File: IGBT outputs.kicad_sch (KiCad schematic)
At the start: 8 parts, among them Q1 NGD8201AN, Q2 NGD8201AN, Q3 NGD8201AN, Q4 NGD8201AN, Q5 NGD8201AN, Q6 NGD8201AN, Q7 NGD8201AN, Q8 NGD8201AN

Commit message: All fixed up for JLC
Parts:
- Q1, Q2, Q3, Q4, Q6, Q7, Q8: LCSC (none) -> C151649
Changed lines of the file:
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@@
+      (effects (font (size 1.27 1.27)) hide)
+    )
+    (property "LCSC" "C151649" (id 4) (at 139.7 119.38 0)
       (effects (font (size 1.27 1.27)) hide)
     )
@@
       (effects (font (size 1.27 1.27)) hide)
     )
+    (property "LCSC" "C151649" (id 4) (at 152.4 81.28 0)
+      (effects (font (size 1.27 1.27)) hide)
+    )
     (pin "1")
     (pin "2")
@@
     )
     (property "Datasheet" "~" (id 3) (at 139.7 64.77 0)
+      (effects (font (size 1.27 1.27)) hide)
+    )
+    (property "LCSC" "C151649" (id 4) (at 139.7 64.77 0)
       (effects (font (size 1.27 1.27)) hide)
     )
@@
       (effects (font (size 1.27 1.27)) hide)
     )
+    (property "LCSC" "C151649" (id 4) (at 139.7 99.06 0)
+      (effects (font (size 1.27 1.27)) hide)
+    )
     (pin "1")
     (pin "2")
@@
       (effects (font (size 1.27 1.27)) hide)
     )
+    (property "LCSC" "C151649" (id 4) (at 139.7 81.28 0)
+      (effects (font (size 1.27 1.27)) hide)
+    )
     (pin "1")
     (pin "2")
@@
     )
     (property "Datasheet" "~" (id 3) (at 152.4 99.06 0)
+      (effects (font (size 1.27 1.27)) hide)
+    )
+    (property "LCSC" "C151649" (id 4) (at 152.4 99.06 0)
       (effects (font (size 1.27 1.27)) hide)
     )
@@
       (effects (font (size 1.27 1.27)) hide)
     )
+    (property "LCSC" "C151649" (id 4) (at 152.4 119.38 0)
+      (effects (font (size 1.27 1.27)) hide)
+    )

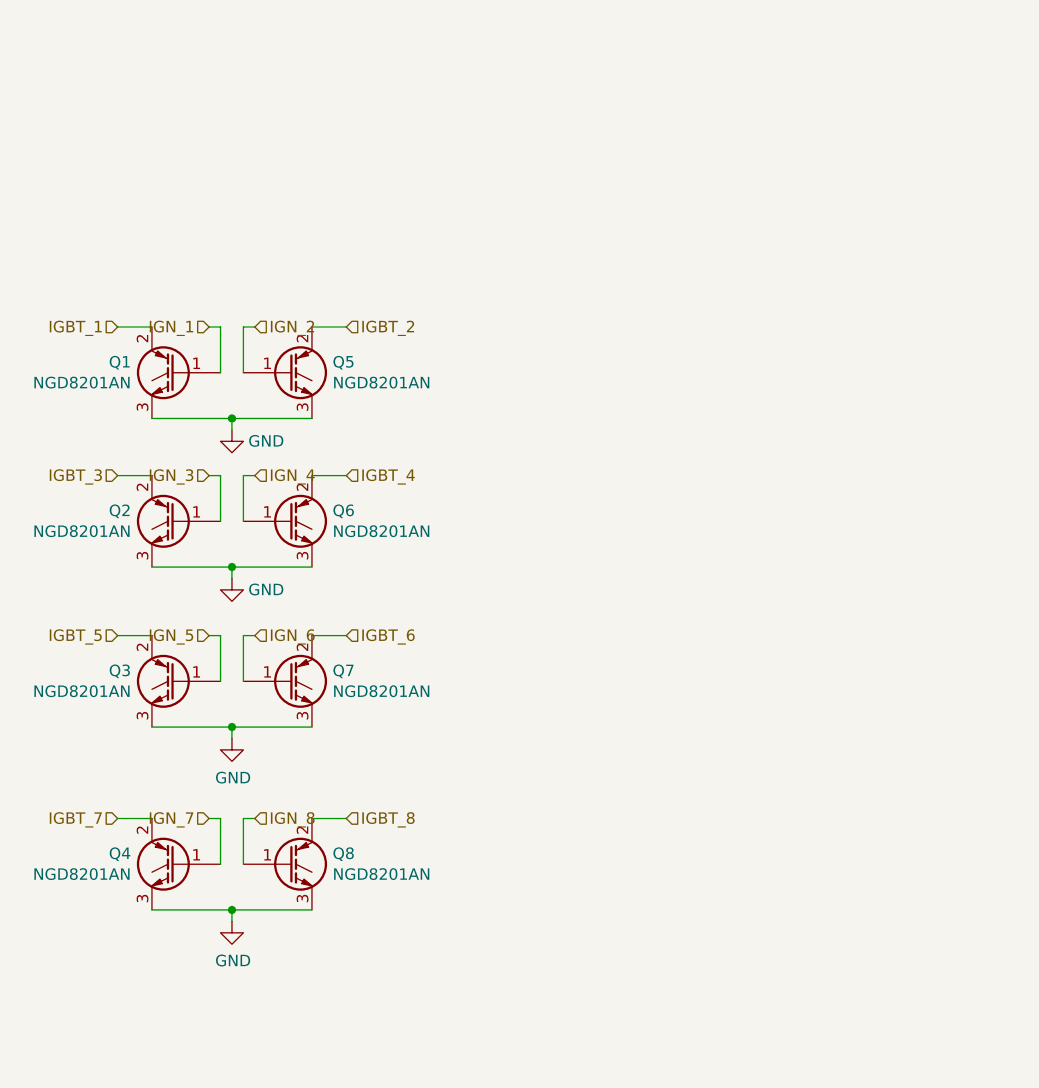
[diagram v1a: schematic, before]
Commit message: convert to kicad7, add jumpers for direct drive igbt output
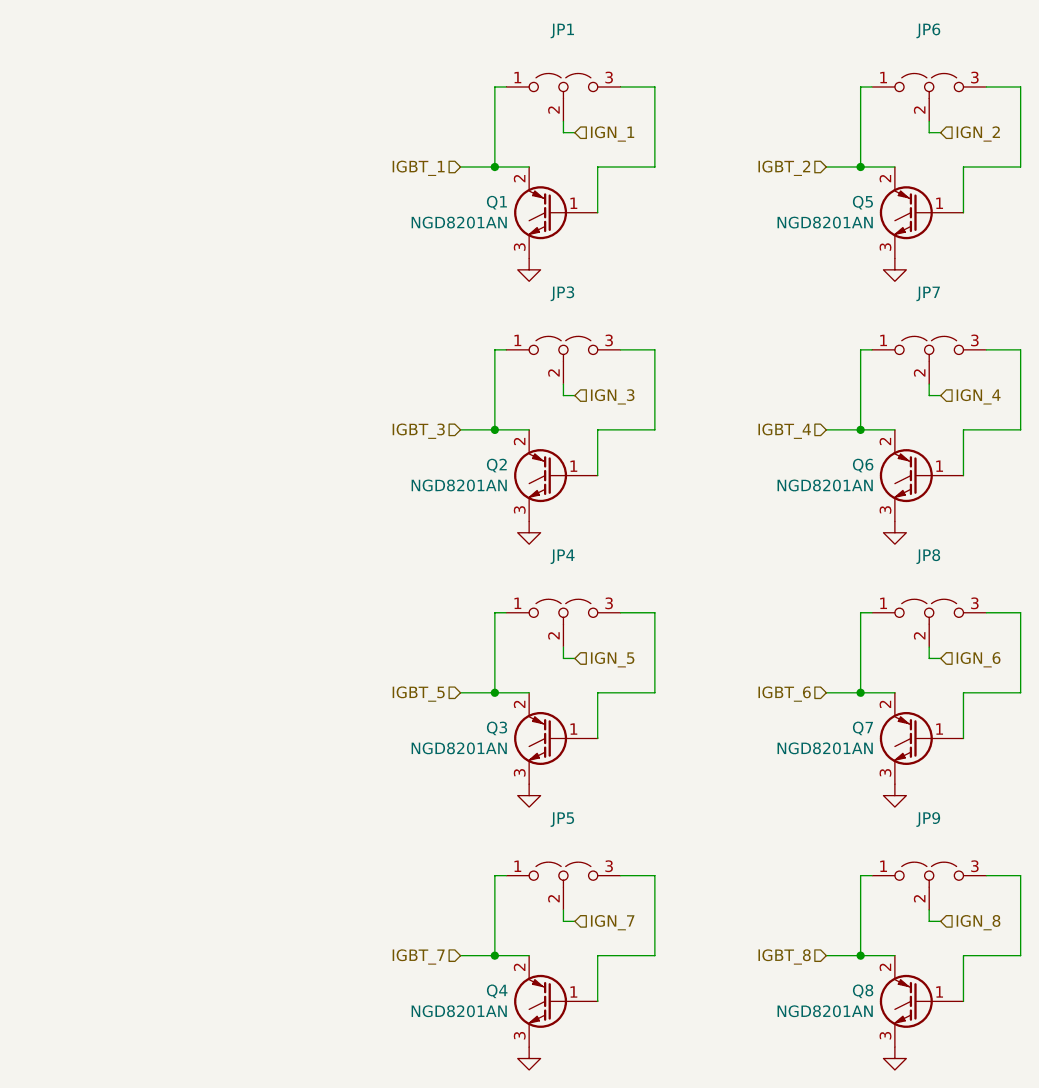
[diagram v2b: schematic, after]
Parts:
- added JP1, JP3, JP4, JP5, JP6, JP7, JP8, JP9: Jumper_3_Open, Jumper:SolderJumper-3_P2.0mm_Open_TrianglePad1.0x1.5mm, symbol Jumper:Jumper_3_Open
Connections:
- net IGBT_1: now also JP1.1 (A)
- net IGBT_2: now also JP6.1 (A)
- net IGBT_3: now also JP3.1 (A)
- net IGBT_4: now also JP7.1 (A)
- net IGBT_5: now also JP4.1 (A)
- net IGBT_6: now also JP8.1 (A)
- net IGBT_7: now also JP5.1 (A)
- net IGBT_8: now also JP9.1 (A)
- net IGN_1: now also JP1.2 (C); no longer Q1.1 (G)
- net IGN_2: now also JP6.2 (C); no longer Q5.1 (G)
- net IGN_3: now also JP3.2 (C); no longer Q2.1 (G)
- net IGN_4: now also JP7.2 (C); no longer Q6.1 (G)
- net IGN_5: now also JP4.2 (C); no longer Q3.1 (G)
- net IGN_6: now also JP8.2 (C); no longer Q7.1 (G)
- net IGN_7: now also JP5.2 (C); no longer Q4.1 (G)
- net IGN_8: now also JP9.2 (C); no longer Q8.1 (G)
- new net: JP5.3 (B), Q4.1 (G)
- new net: JP7.3 (B), Q6.1 (G)
- new net: JP1.3 (B), Q1.1 (G)
- new net: JP3.3 (B), Q2.1 (G)
- new net: JP4.3 (B), Q3.1 (G)
- new net: JP8.3 (B), Q7.1 (G)
- new net: JP9.3 (B), Q8.1 (G)
- new net: JP6.3 (B), Q5.1 (G)
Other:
- moved on the sheet: Q1, Q2, Q3, Q4, Q5, Q6, Q7, Q8
